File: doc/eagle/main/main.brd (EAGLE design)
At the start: 77.1 x 62.2 mm, 27 parts, among them U1 168A-PU

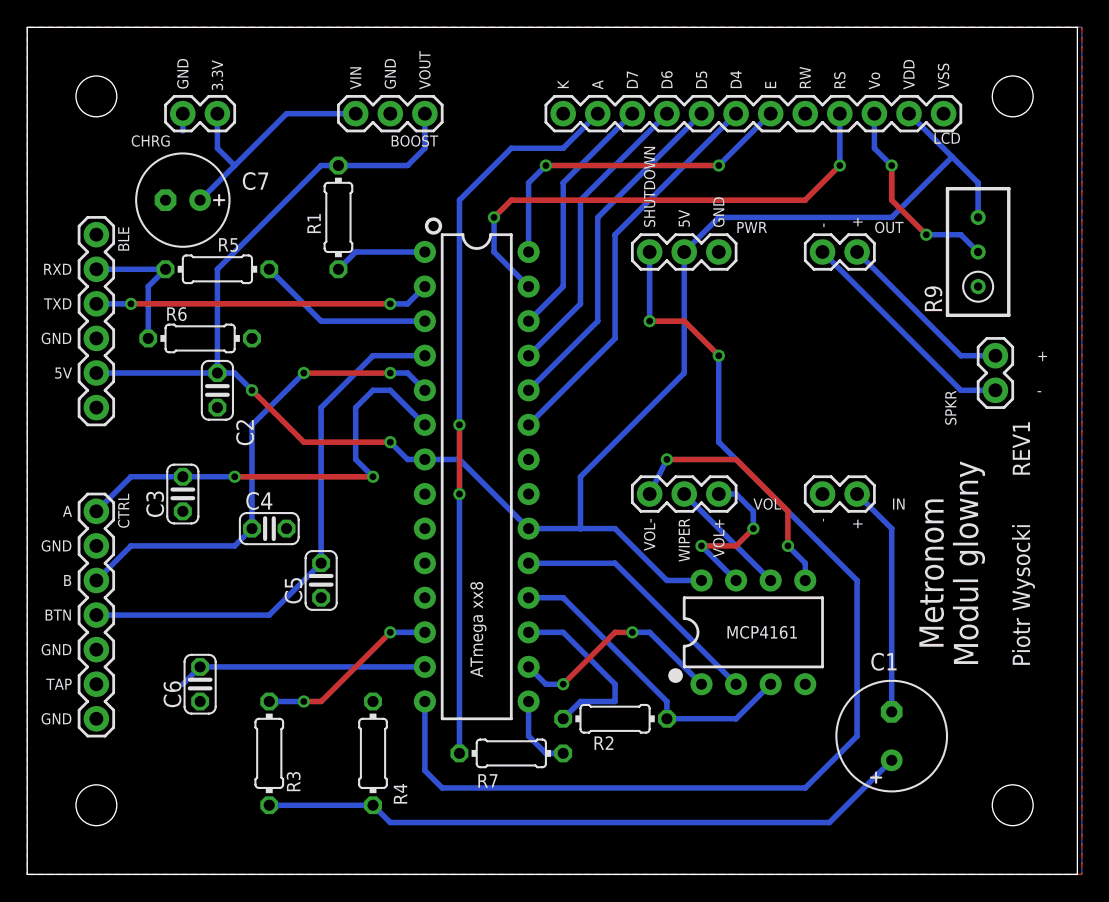
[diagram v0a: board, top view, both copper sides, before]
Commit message: Storing metronome params in EEPROM after user inactivity, Eagle files + PDF exports
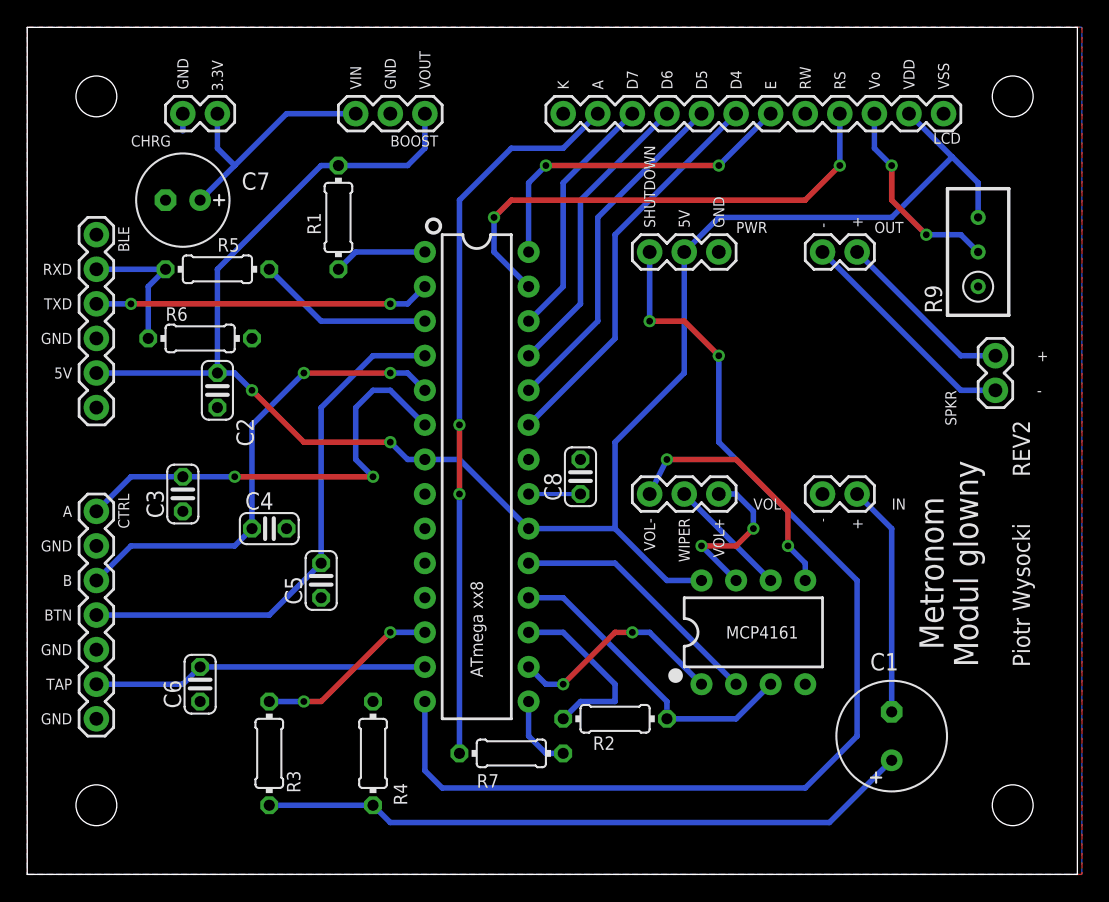
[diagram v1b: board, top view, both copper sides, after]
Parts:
- added C8: 100n, rcl:C025-024X044
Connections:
- new net N$6: C8.1, U1.21
- net GND: now also C8.2
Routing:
- net TAP: track 18.3 -> 24.7 mm
- net N$6: track 0.00 -> 3.81 mm
- net 5V: track 135.6 -> 134.6 mm
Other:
- board text added: "REV2"
- board text removed: "REV1"
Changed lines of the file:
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@@
 <?xml version="1.0" encoding="utf-8"?>
 <!DOCTYPE eagle SYSTEM "eagle.dtd">
-<eagle version="7.7.0">
+<eagle version="9.2.2">
 <drawing>
 <settings>
 <setting alwaysvectorfont="no"/>
+<setting keepoldvectorfont="yes"/>
 <setting verticaltext="up"/>
 </settings>
@@
 <text x="71.12" y="29.21" size="1.778" layer="21" font="vector" rot="R90">Modul glowny</text>
 <text x="74.93" y="29.21" size="1.27" layer="21" font="vector" rot="R90">Piotr Wysocki</text>
-<text x="74.93" y="43.18" size="1.27" layer="21" font="vector" rot="R90">REV1</text>
+<text x="74.93" y="43.18" size="1.27" layer="21" font="vector" rot="R90">REV2</text>
 <text x="25.4" y="71.628" size="0.8128" layer="25" font="vector" ratio="20" distance="63" rot="R90" align="center-left">VIN</text>
 <text x="27.94" y="71.628" size="0.8128" layer="25" font="vector" ratio="20" distance="63" rot="R90" align="center-left">GND</text>
@@
 <attribute name="VALUE" x="53.34" y="43.942" size="0.6096" layer="27" font="vector" ratio="20" rot="R180"/>
 </element>
+<element name="C8" library="rcl" package="C025-024X044" value="100n" x="41.91" y="43.18" smashed="yes" rot="R90">
+<attribute name="NAME" x="40.513" y="41.402" size="1.27" layer="25" ratio="10" rot="R90"/>
+<attribute name="SPICEPREFIX" value="C" x="41.91" y="43.18" size="1.778" layer="27" rot="R90" display="off"/>
+<attribute name="VALUE" x="44.577" y="41.402" size="1.27" layer="27" ratio="10" rot="R90"/>
+</element>
 </elements>
 <signals>
@@
 <wire x1="12.7" y1="68.58" x2="12.7" y2="69.85" width="0.4064" layer="16"/>
 <contactref element="IN" pad="2"/>
+<contactref element="C8" pad="2"/>
 </signal>
 <signal name="N$3">
@@
 <contactref element="R9" pad="3"/>
 <contactref element="BOOST" pad="3"/>
-<wire x1="38.1" y1="39.37" x2="41.91" y2="39.37" width="0.4064" layer="16"/>
-<wire x1="41.91" y1="39.37" x2="44.45" y2="39.37" width="0.4064" layer="16"/>
+<wire x1="38.1" y1="39.37" x2="44.45" y2="39.37" width="0.4064" layer="16"/>
 <wire x1="48.26" y1="35.56" x2="50.8" y2="35.56" width="0.4064" layer="16"/>
 <wire x1="48.26" y1="35.56" x2="44.45" y2="39.37" width="0.4064" layer="16"/>
@@
 <wire x1="64.77" y1="62.23" x2="52.07" y2="62.23" width="0.4064" layer="16"/>
 <wire x1="64.77" y1="62.23" x2="69.215" y2="66.675" width="0.4064" layer="16"/>
-<wire x1="41.91" y1="43.18" x2="49.53" y2="50.8" width="0.4064" layer="16"/>
-<wire x1="41.91" y1="43.18" x2="41.91" y2="39.37" width="0.4064" layer="16"/>
+<wire x1="44.45" y1="45.72" x2="49.53" y2="50.8" width="0.4064" layer="16"/>
+<wire x1="44.45" y1="45.72" x2="44.45" y2="39.37" width="0.4064" layer="16"/>
 <wire x1="49.53" y1="50.8" x2="49.53" y2="59.69" width="0.4064" layer="16"/>
 <wire x1="52.07" y1="62.23" x2="49.53" y2="59.69" width="0.4064" layer="16"/>
@@
 <contactref element="C6" pad="2"/>
 <contactref element="U1" pad="13"/>
-<wire x1="12.7" y1="27.94" x2="13.97" y2="29.21" width="0.4064" layer="16"/>
+<wire x1="13.97" y1="29.21" x2="12.7" y2="27.94" width="0.4064" layer="16"/>
 <wire x1="13.97" y1="29.21" x2="30.48" y2="29.21" width="0.4064" layer="16"/>
 <contactref element="CTRL" pad="6"/>
-<wire x1="6.35" y1="27.94" x2="12.7" y2="27.94" width="0" layer="19" extent="16-16"/>
+<wire x1="12.7" y1="27.94" x2="6.35" y2="27.94" width="0.4064" layer="16"/>
 </signal>
 <signal name="RXD">
@@
 <wire x1="64.77" y1="39.37" x2="64.77" y2="25.908" width="0.4064" layer="16"/>
 </signal>
+<signal name="N$6">
+<contactref element="C8" pad="1"/>
+<contactref element="U1" pad="21"/>
+<wire x1="38.1" y1="41.91" x2="41.91" y2="41.91" width="0.3048" layer="16"/>
+</signal>
 </signals>
